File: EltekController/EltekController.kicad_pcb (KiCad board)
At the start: 2 copper layers, 65 x 37.5 mm, 36 parts, among them J1 CANBUS, J2 ESP-PROG, J3 Qwiic, SW1 RST, SW2 BOOT, SW3 LEFT, SW4 SEL, SW5 RIGHT, U1 ESP32-S2-WROVER, U2 MAX3051ESA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

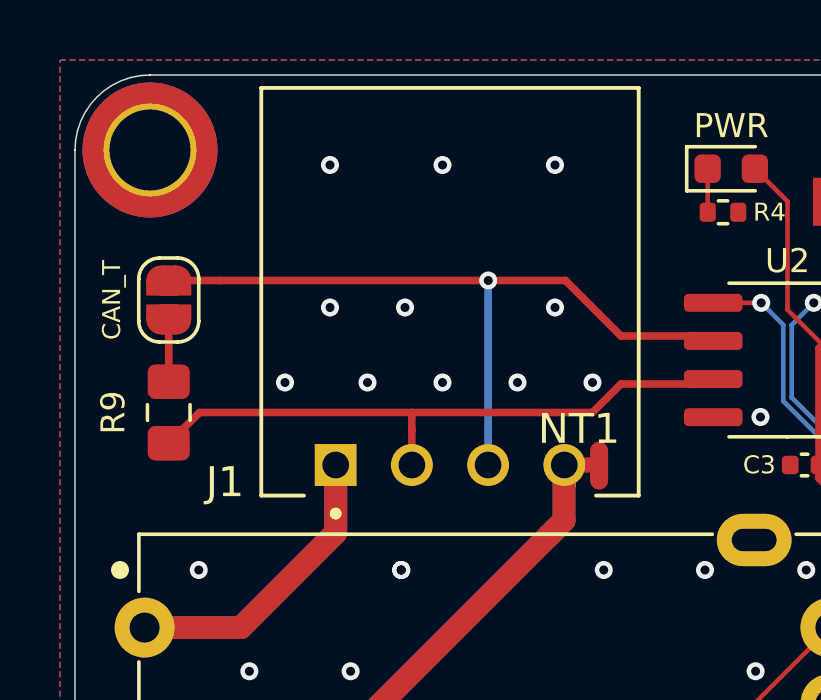
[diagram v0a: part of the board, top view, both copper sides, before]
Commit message: switch to nano-fit, but any 2.54 or 2.5mm header works
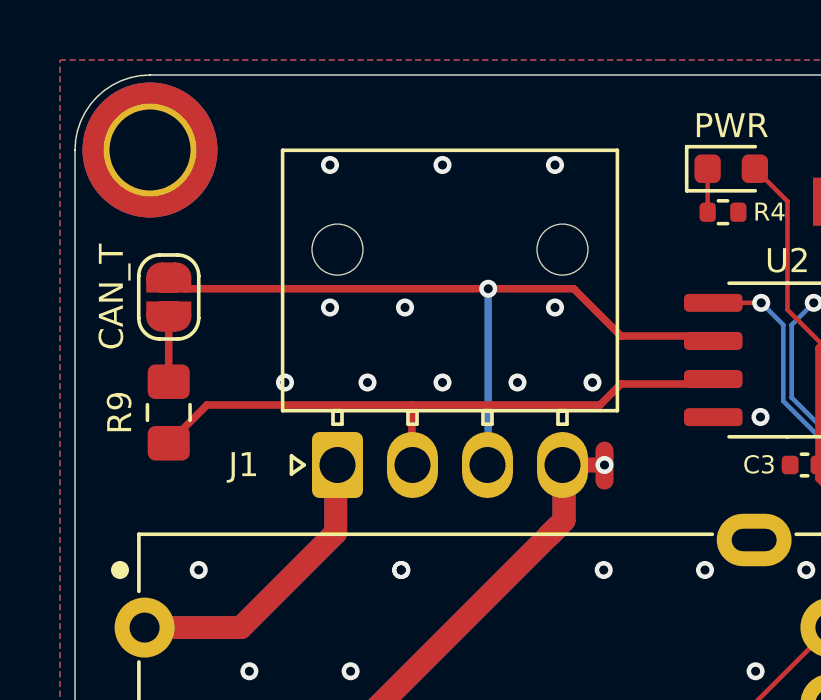
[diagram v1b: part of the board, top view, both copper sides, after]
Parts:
- J1: footprint SnapEDA-zip:TE_5-103634-3 -> 11-My-Edits:Molex_Nano-Fit_105313-xx04_1x04_P2.50mm_Horizontal_3D
- moved NT1 0.35 mm to (117.2, 90.0)
- moved JP2 0.10 mm to (103.1, 84.4)
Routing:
- net GND: vias 72 -> 73

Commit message: missed a trace
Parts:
- moved R9 0.62 mm to (103.1, 87.6), turned to 180 degrees
- moved JP2 0.35 mm to (103.1, 84.8)
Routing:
- net /CAN+: track 21.3 -> 19.9 mm
- net /CAN-: track 25.0 -> 24.4 mm

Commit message: micro-usb footprint fixup
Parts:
- moved USB1 1.00 mm to (128.8, 79.0)
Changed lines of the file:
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@@
     (46 B.CrtYd user)
     (47 F.CrtYd user)
-    (49 F.Fab user hide)
+    (49 F.Fab user)
   )
   (setup
@@
   )
   (module 41-EasyEDA-Edits:MICRO-USB-SMD_U254-051T-4BH83-F1S_C397452 (layer Front)
-    (at 128.75 80 180)
+    (at 128.75 79 180)
     (attr smd)
     (fp_text reference USB1 (at 0 -3) (layer F.SilkS)
@@
       (effects (font (size 0.5 0.5) (thickness 0.08)))
     )
-    (fp_line (start -3.75 4.325) (end -3.75 -1.55) (layer F.Fab) (width 0.1))
-    (fp_line (start 4.4 -2.46) (end 4.4 4.5) (layer F.CrtYd) (width 0.05))
-    (fp_line (start -1.1 -1.9625) (end -1.3 -1.7625) (layer F.Fab) (width 0.1))
-    (fp_line (start -1.5 -2.1) (end -1.5 -1.9625) (layer F.Fab) (width 0.1))
-    (fp_line (start -3.75 4.325) (end 3.75 4.325) (layer F.Fab) (width 0.1))
-    (fp_line (start -1.5 -2.1) (end -1.1 -2.1) (layer F.Fab) (width 0.1))
-    (fp_line (start -1.1 -2.1) (end -1.1 -1.9625) (layer F.Fab) (width 0.1))
-    (fp_line (start -1.7 -2.3) (end -1.3 -2.3) (layer F.SilkS) (width 0.12))
-    (fp_line (start 3.8 2.8) (end 3.8 -0.25) (layer F.SilkS) (width 0.12))
-    (fp_line (start -3.75 -1.55) (end 3.75 -1.55) (layer F.Fab) (width 0.1))
-    (fp_line (start -3 3) (end 3 3) (layer Dwgs.User) (width 0.1))
-    (fp_line (start 3.75 4.325) (end 3.75 -1.55) (layer F.Fab) (width 0.1))
-    (fp_line (start -1.7 -2.3) (end -1.7 -1.85) (layer F.SilkS) (width 0.12))
-    (fp_line (start -4.4 4.5) (end -4.4 -2.46) (layer F.CrtYd) (width 0.05))
-    (fp_line (start 3.8 -2.2) (end 1.9 -2.2) (layer F.SilkS) (width 0.12))
-    (fp_line (start -4.4 4.5) (end 4.4 4.5) (layer F.CrtYd) (width 0.05))
-    (fp_line (start -4.4 -2.46) (end 4.4 -2.46) (layer F.CrtYd) (width 0.05))
-    (fp_line (start -1.3 -1.7625) (end -1.5 -1.9625) (layer F.Fab) (width 0.1))
-    (fp_line (start -3.8 2.8) (end -3.8 -0.25) (layer F.SilkS) (width 0.12))
-    (fp_line (start 1.9 -1.85) (end 1.9 -2.2) (layer F.SilkS) (width 0.12))
-    (fp_line (start -1.9 -1.85) (end -1.9 -2.2) (layer F.SilkS) (width 0.12))
-    (fp_line (start -1.9 -2.2) (end -3.8 -2.2) (layer F.SilkS) (width 0.12))
-    (fp_line (start -3.8 -2.2) (end -3.8 -2.15) (layer F.SilkS) (width 0.12))
-    (fp_line (start 3.8 -2.2) (end 3.8 -2.15) (layer F.SilkS) (width 0.12))
-    (pad 1 smd rect (at -1.3 -1.325 180) (size 0.4 1.4) (layers Front F.Paste F.Mask)
+    (fp_line (start 3.8 -3.2) (end 3.8 -3.15) (layer F.SilkS) (width 0.12))
+    (fp_line (start -3.8 -3.2) (end -3.8 -3.15) (layer F.SilkS) (width 0.12))
+    (fp_line (start -1.9 -3.2) (end -3.8 -3.2) (layer F.SilkS) (width 0.12))
+    (fp_line (start -1.9 -2.85) (end -1.9 -3.2) (layer F.SilkS) (width 0.12))
+    (fp_line (start 1.9 -2.85) (end 1.9 -3.2) (layer F.SilkS) (width 0.12))
+    (fp_line (start -3.8 1.8) (end -3.8 -1.25) (layer F.SilkS) (width 0.12))
+    (fp_line (start -1.3 -2.7625) (end -1.5 -2.9625) (layer F.Fab) (width 0.1))
+    (fp_line (start -4.4 -3.46) (end 4.4 -3.46) (layer F.CrtYd) (width 0.05))
+    (fp_line (start -4.4 3.5) (end 4.4 3.5) (layer F.CrtYd) (width 0.05))
+    (fp_line (start 3.8 -3.2) (end 1.9 -3.2) (layer F.SilkS) (width 0.12))
+    (fp_line (start -4.4 3.5) (end -4.4 -3.46) (layer F.CrtYd) (width 0.05))
+    (fp_line (start -1.7 -3.3) (end -1.7 -2.85) (layer F.SilkS) (width 0.12))
+    (fp_line (start 3.75 3.325) (end 3.75 -2.55) (layer F.Fab) (width 0.1))
+    (fp_line (start -3 2) (end 3 2) (layer Dwgs.User) (width 0.1))
+    (fp_line (start -3.75 -2.55) (end 3.75 -2.55) (layer F.Fab) (width 0.1))
+    (fp_line (start 3.8 1.8) (end 3.8 -1.25) (layer F.SilkS) (width 0.12))
+    (fp_line (start -1.7 -3.3) (end -1.3 -3.3) (layer F.SilkS) (width 0.12))
+    (fp_line (start -1.1 -3.1) (end -1.1 -2.9625) (layer F.Fab) (width 0.1))
+    (fp_line (start -1.5 -3.1) (end -1.1 -3.1) (layer F.Fab) (width 0.1))
+    (fp_line (start -3.75 3.325) (end 3.75 3.325) (layer F.Fab) (width 0.1))
+    (fp_line (start -1.5 -3.1) (end -1.5 -2.9625) (layer F.Fab) (width 0.1))
+    (fp_line (start -1.1 -2.9625) (end -1.3 -2.7625) (layer F.Fab) (width 0.1))
+    (fp_line (start 4.4 -3.46) (end 4.4 3.5) (layer F.CrtYd) (width 0.05))
+    (fp_line (start -3.75 3.325) (end -3.75 -2.55) (layer F.Fab) (width 0.1))
+    (pad 1 smd rect (at -1.3 -2.325 180) (size 0.4 1.4) (layers Front F.Paste F.Mask)
       (net 12 /VBUS))
-    (pad 2 smd rect (at -0.65 -1.325 180) (size 0.4 1.4) (layers Front F.Paste F.Mask)
+    (pad 2 smd rect (at -0.65 -2.325 180) (size 0.4 1.4) (layers Front F.Paste F.Mask)
       (net 13 /USB_D-))
-    (pad 3 smd rect (at 0 -1.325 180) (size 0.4 1.4) (layers Front F.Paste F.Mask)
+    (pad 3 smd rect (at 0 -2.325 180) (size 0.4 1.4) (layers Front F.Paste F.Mask)
       (net 11 /USB_D+))
-    (pad 4 smd rect (at 0.65 -1.325 180) (size 0.4 1.4) (layers Front F.Paste F.Mask)
+    (pad 4 smd rect (at 0.65 -2.325 180) (size 0.4 1.4) (layers Front F.Paste F.Mask)
       (net 34 /USB_ID))
-    (pad 5 smd rect (at 1.3 -1.325 180) (size 0.4 1.4) (layers Front F.Paste F.Mask)
-      (net 2 GND))
-    (pad 6 smd rect (at 3.1 -1.225 270) (size 1.6 2.1) (layers Front F.Paste F.Mask)
-      (net 2 GND))
-    (pad 6 smd rect (at -3.1 -1.225 270) (size 1.6 2.1) (layers Front F.Paste F.Mask)
-      (net 2 GND))
-    (pad 6 thru_hole oval (at -2.83 1.325 180) (size 1.5 2) (drill oval 0.9 1.4) (layers *.Cu *.Paste *.Mask)
-      (net 2 GND))
-    (pad 6 thru_hole oval (at 2.83 1.325 180) (size 1.5 2) (drill oval 0.9 1.4) (layers *.Cu *.Paste *.Mask)
-      (net 2 GND))
-    (pad "" np_thru_hole circle (at 2 -1.025 180) (size 0.5 0.5) (drill 0.45) (layers *.Cu *.Mask))
-    (pad "" np_thru_hole circle (at -2 -1.025 180) (size 0.45 0.45) (drill 0.45) (layers *.Cu *.Mask))
+    (pad 5 smd rect (at 1.3 -2.325 180) (size 0.4 1.4) (layers Front F.Paste F.Mask)
+      (net 2 GND))
+    (pad 6 smd rect (at 3.1 -2.225 270) (size 1.6 2.1) (layers Front F.Paste F.Mask)
+      (net 2 GND))
+    (pad 6 smd rect (at -3.1 -2.225 270) (size 1.6 2.1) (layers Front F.Paste F.Mask)
+      (net 2 GND))
+    (pad 6 thru_hole oval (at -2.83 0.325) (size 1.5 2) (drill oval 0.9 1.4) (layers *.Cu *.Paste *.Mask)
+      (net 2 GND))
+    (pad 6 thru_hole oval (at 2.83 0.325 180) (size 1.5 2) (drill oval 0.9 1.4) (layers *.Cu *.Paste *.Mask)
+      (net 2 GND))
+    (pad "" np_thru_hole circle (at 2 -2.025 180) (size 0.5 0.5) (drill 0.45) (layers *.Cu *.Mask))
+    (pad "" np_thru_hole circle (at -2 -2.025 180) (size 0.45 0.45) (drill 0.45) (layers *.Cu *.Mask))
     (model ${EASY_EDA_3D}/EasyEDA.3dshapes/MICRO-USB-SMD_U254-051T-4BH83-F1S.wrl
-      (offset (xyz 0 -1 1.25))
+      (offset (xyz 0 0 1.25))
       (scale (xyz 0.3937 0.3937 0.3937))
       (rotate (xyz 0 0 0))
@@
   (segment (start 130.2835 80.05) (end 134.325 80.05) (width 0.254) (layer Front) (net 12))
   (segment (start 130.05 80.2835) (end 130.2835 80.05) (width 0.254) (layer Front) (net 12))
-  (segment (start 130.05 81.2125) (end 130.05 80.2835) (width 0.254) (layer Front) (net 12))
-  (segment (start 134.44 94.99) (end 134.75 94.99) (width 0.1524) (layer Front) (net 13))
+  (segment (start 130.05 81.325) (end 130.05 80.2835) (width 0.254) (layer Front) (net 12))
   (segment (start 133.85 95.58) (end 134.44 94.99) (width 0.1524) (layer Front) (net 13))
-  (segment (start 129.4 82.225001) (end 129.2274 82.397601) (width 0.1524) (layer Front) (net 13))
-  (segment (start 129.4 81.325) (end 129.4 82.225001) (width 0.1524) (layer Front) (net 13))
-  (segment (start 129.2274 82.397601) (end 129.2274 92.236872) (width 0.1524) (layer Front) (net 13))
   (segment (start 132.570528 95.58) (end 133.85 95.58) (width 0.1524) (layer Front) (net 13))
   (segment (start 129.2274 92.236872) (end 132.570528 95.58) (width 0.1524) (layer Front) (net 13))
+  (segment (start 134.44 94.99) (end 134.75 94.99) (width 0.1524) (layer Front) (net 13))
+  (segment (start 129.4 82.225001) (end 129.2274 82.397601) (width 0.1524) (layer Front) (net 13))
+  (segment (start 129.2274 82.397601) (end 129.2274 92.236872) (width 0.1524) (layer Front) (net 13))
+  (segment (start 129.4 81.325) (end 129.4 82.225001) (width 0.1524) (layer Front) (net 13))
   (segment (start 149 79.19) (end 149.515 78.675) (width 0.254) (layer Front) (net 14))
   (segment (start 149 85.49) (end 149 79.19) (width 0.254) (layer Front) (net 14))

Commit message: flip VCC and GND on the OLED... sigh
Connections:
- I2C1 pad 1: GND -> +3V3
- I2C1 pad 2: +3V3 -> GND
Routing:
- net +3V3: track 126.9 -> 128.7 mm

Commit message: Revert "flip VCC and GND on the OLED... sigh"
This reverts commit 16d08c3f3e759163bdd9650e3550ba9f731368f2.
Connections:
- I2C1 pad 1: +3V3 -> GND
- I2C1 pad 2: GND -> +3V3
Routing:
- net +3V3: track 128.7 -> 126.9 mm
